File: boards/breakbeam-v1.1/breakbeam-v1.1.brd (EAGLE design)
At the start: 19.7 x 14.2 mm, 5 parts, among them X1 87438-02, X2 87438-02

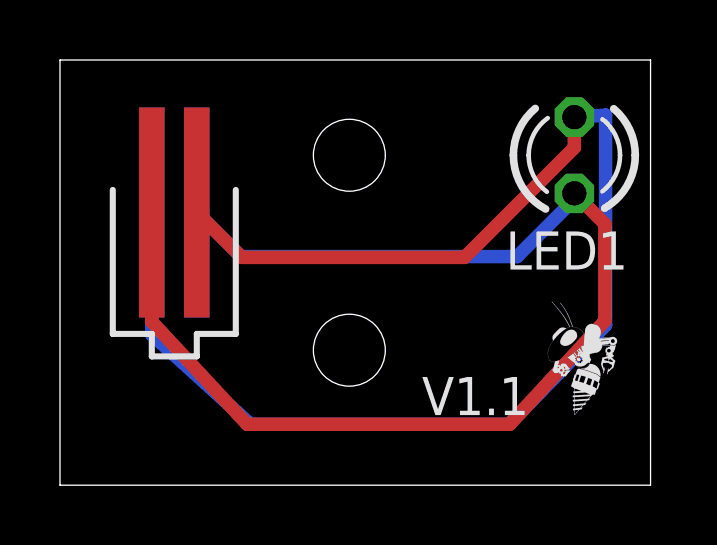
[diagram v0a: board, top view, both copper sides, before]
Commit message: STLs of all boards on the robot are done
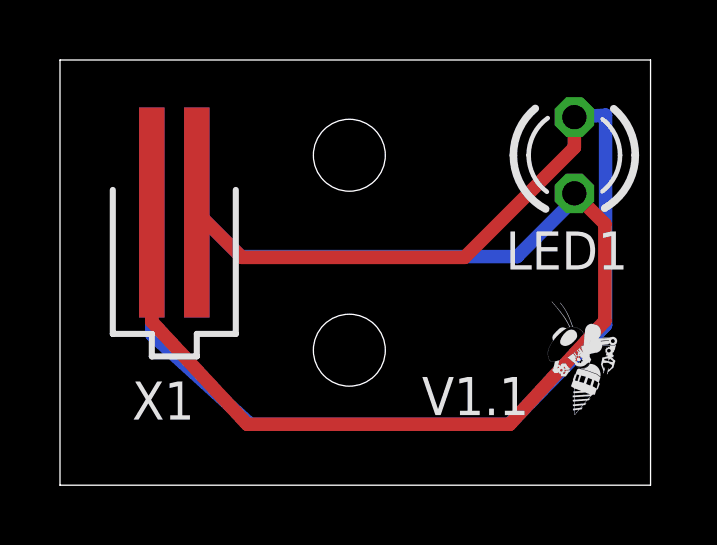
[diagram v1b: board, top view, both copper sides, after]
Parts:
- LED1: device led:LED3MM -> RoboJackets-LEDs:LED3MM
- X1, X2: device con-molex:87438-02 -> RoboJackets-Connectors:87438-02
